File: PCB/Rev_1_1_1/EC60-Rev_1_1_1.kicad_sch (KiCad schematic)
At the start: 28 parts, among them J1 JST, SW1 BOOT0, U1 STM32F401CBUx, U5 XC6206PxxxMR, Y1 8 MHz

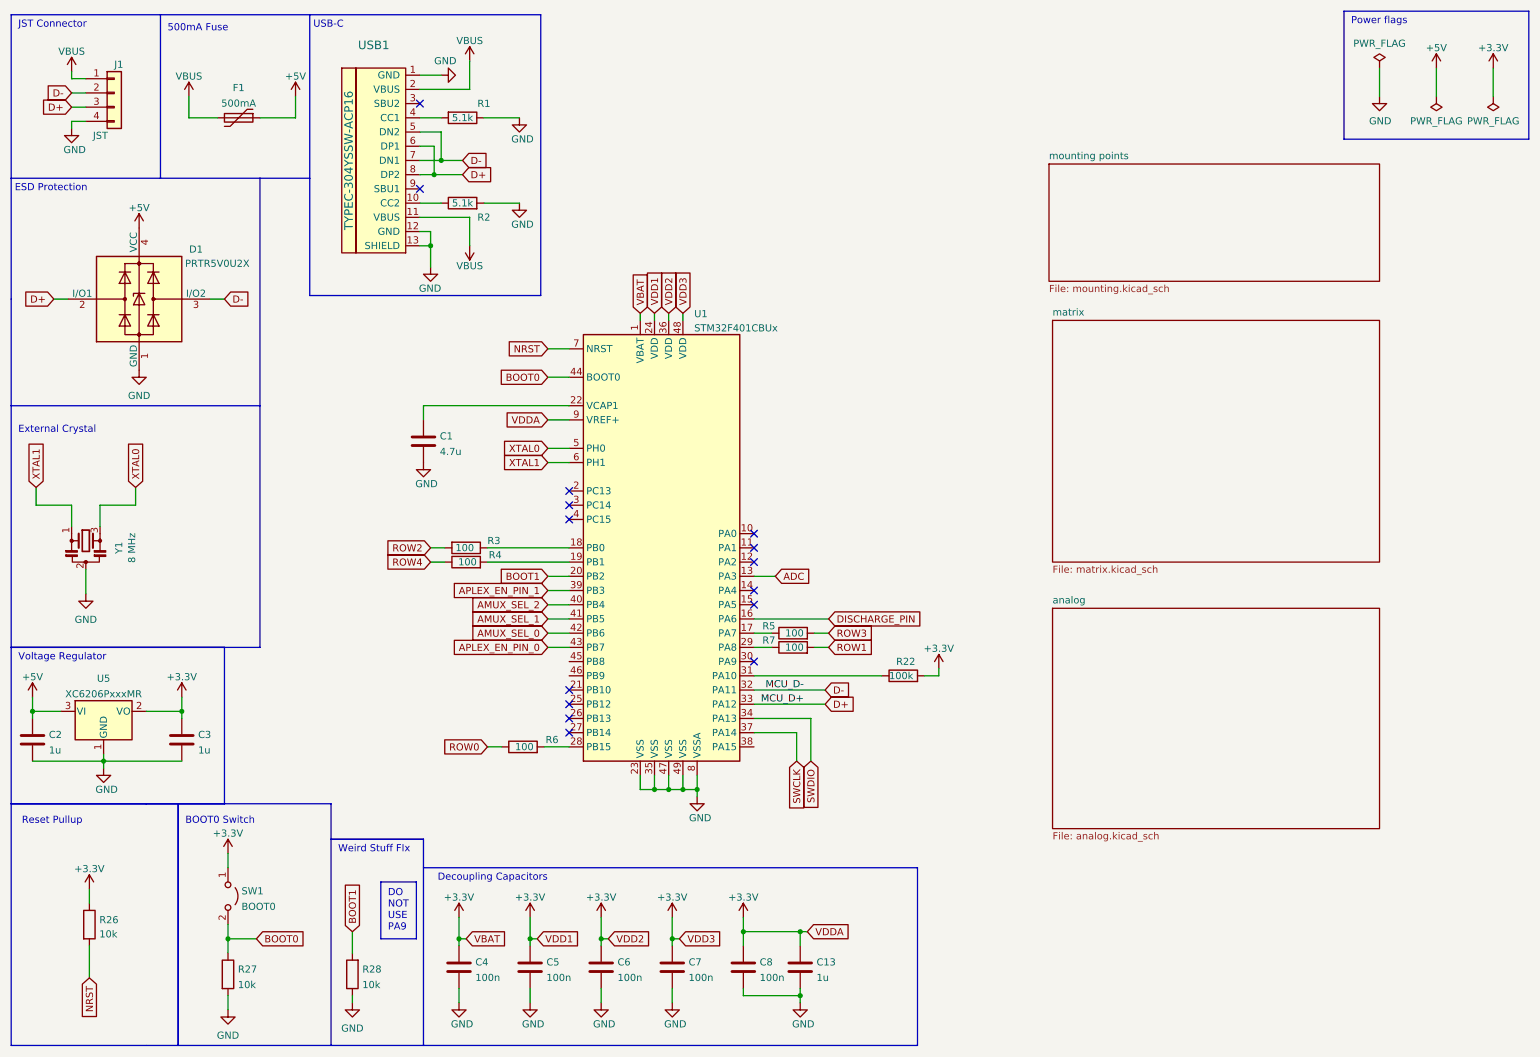
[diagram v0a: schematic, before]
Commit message: Update
Updated the License for the project and relative details.
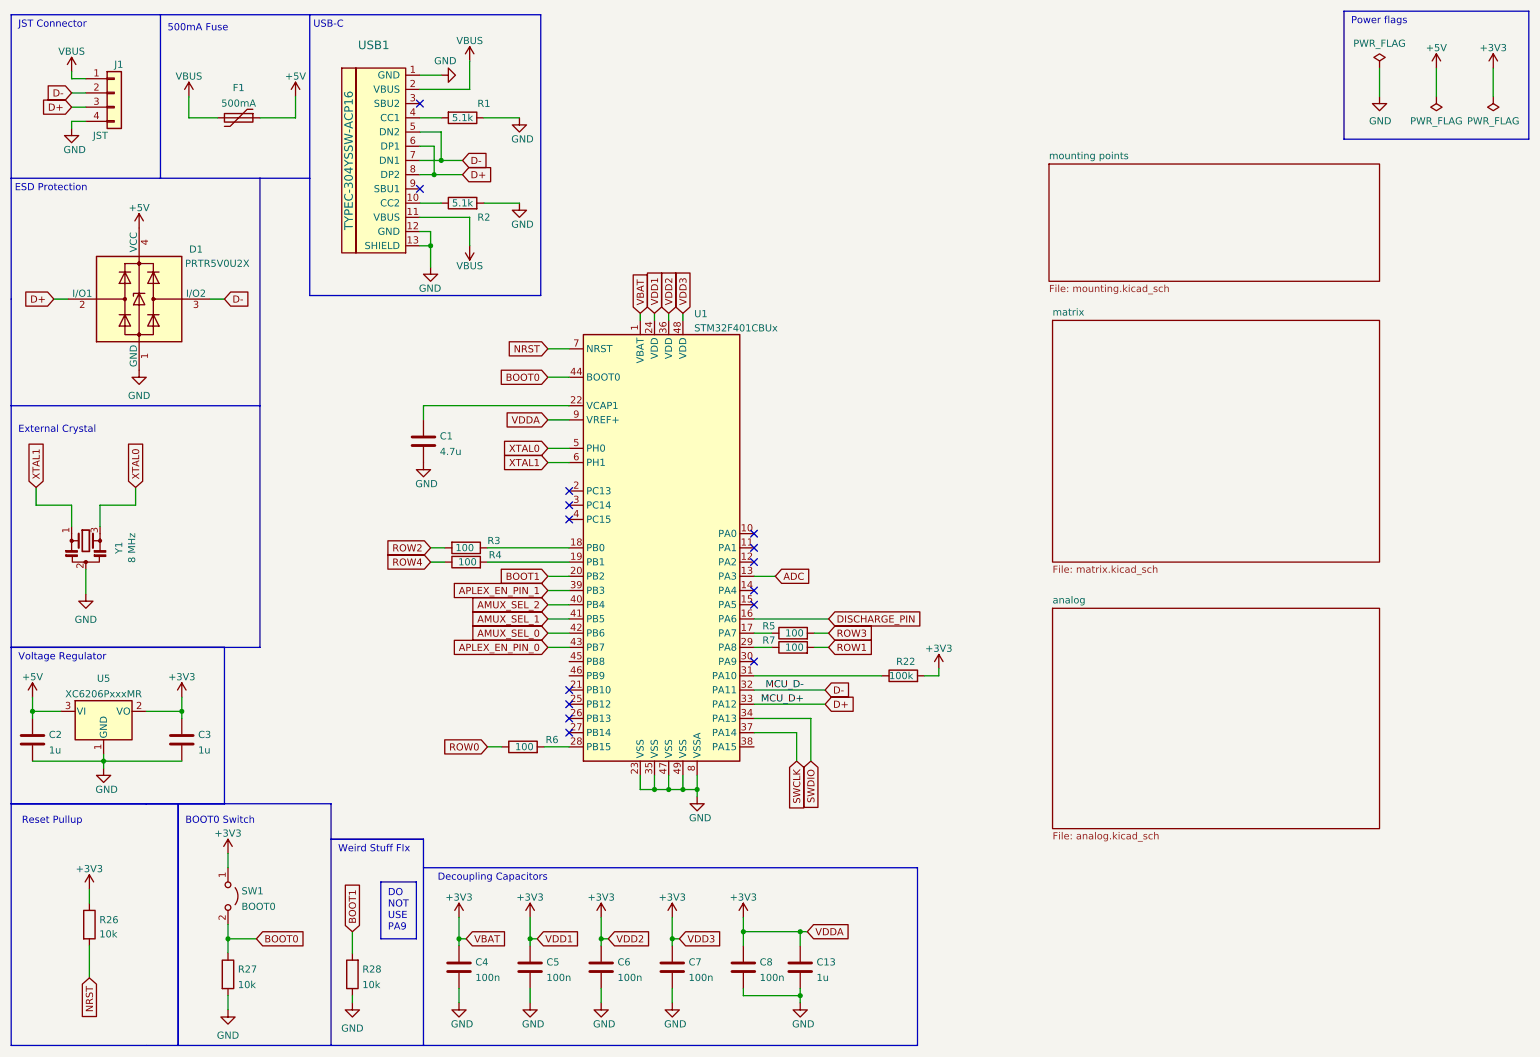
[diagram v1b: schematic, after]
